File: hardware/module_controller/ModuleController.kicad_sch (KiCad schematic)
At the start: 23 parts, among them J1 JST B5B-XH-A, J6 2x08 Edge Connector, U1 ULN2003, U2 A1101ELHL, U3 SN75176AP, U4 ATmega8A-A, Y1 16,0000-HC49U-S

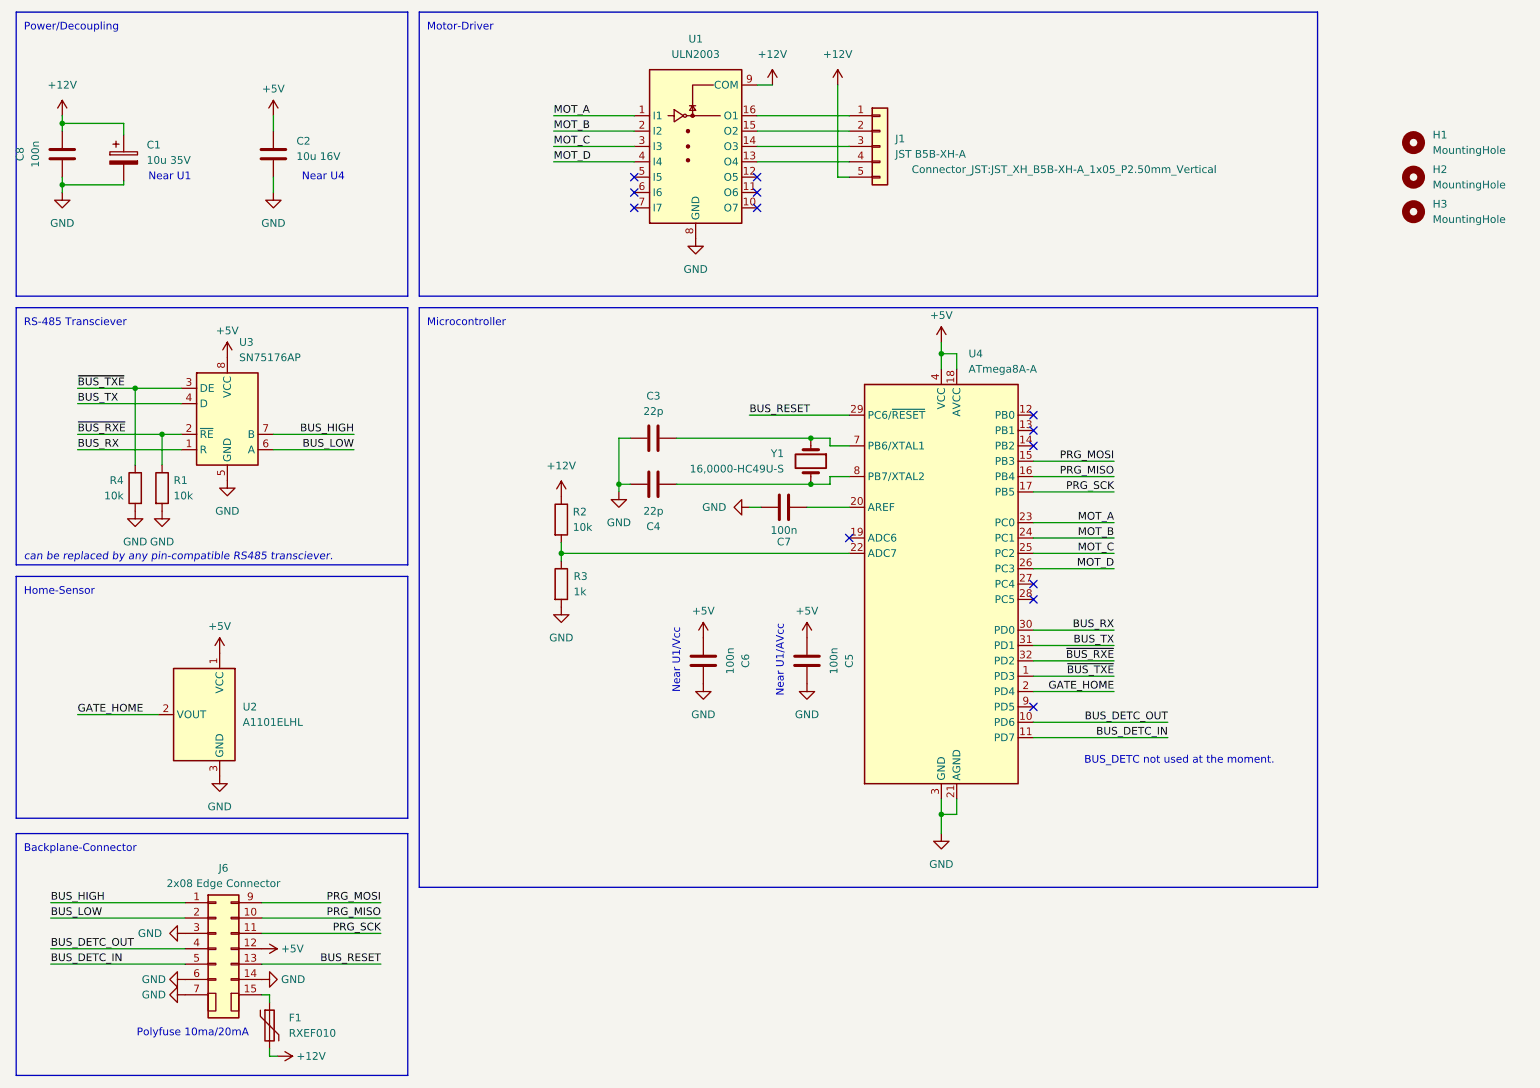
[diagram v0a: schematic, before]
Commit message: updated schematics
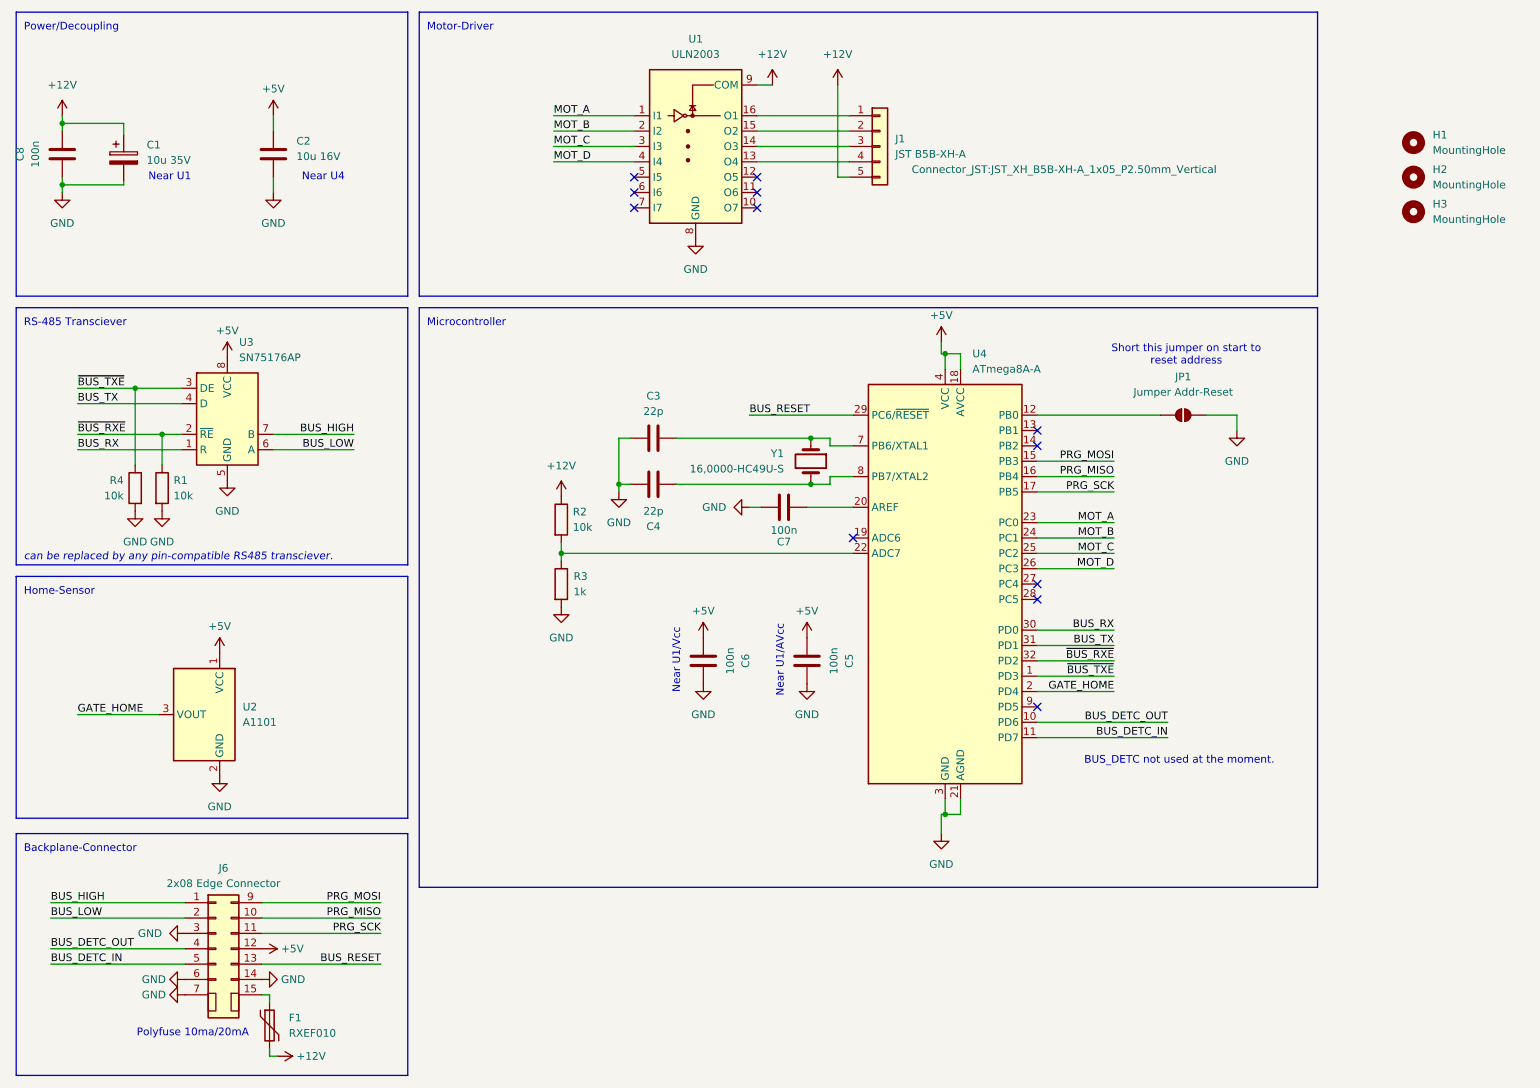
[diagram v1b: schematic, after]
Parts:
- added JP1: Jumper Addr-Reset, Jumper:SolderJumper-2_P1.3mm_Open_Pad1.0x1.5mm, symbol Jumper:SolderJumper_2_Open
- U2: value A1101ELHL -> A1101; footprint Package_TO_SOT_SMD:SOT-23W -> Dennis:UA A1101
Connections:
- net GATE_HOME: now also U2.3 (VOUT); no longer U2.2 (VOUT)
- net GND: now also U2.2 (GND), JP1.2 (B); no longer U2.3 (GND)
- net at U4.12 (PB0): now also JP1.1 (A)
- no-connect marks 13 -> 12
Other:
- note added: "Short this jumper on start to reset address"
- moved on the sheet: U4
